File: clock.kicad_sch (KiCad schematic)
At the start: 54 parts, among them J1 USB_C_Receptacle_USB2.0_16P, J2 Conn_01x02_Pin, J4 Conn_01x02_Pin, J5 Battery, Q1 NMOS-SI2302, Q2 NPN, SW1 SW_SPST, SW2 SW_SPST, SW4 SW_SPDT, SW5 SW_SPST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

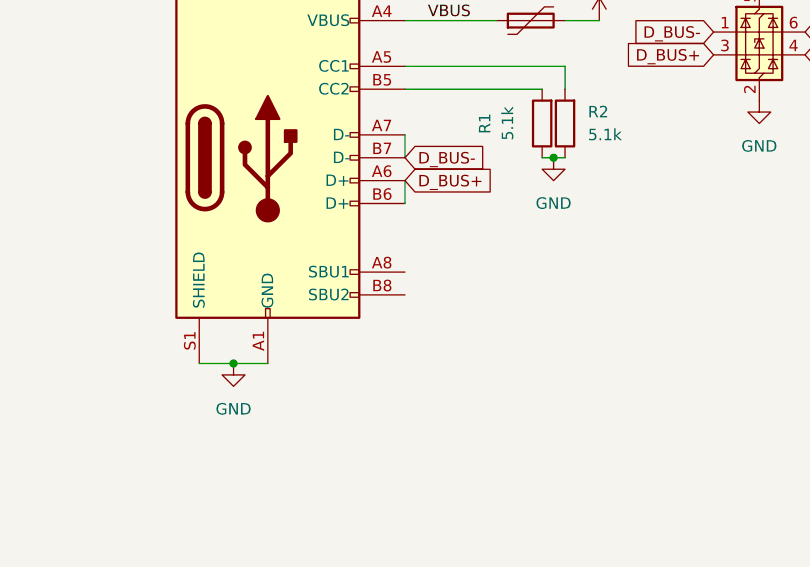
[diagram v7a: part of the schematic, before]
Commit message: sent off for production, added a few GND vias, put NRST and BOOT silkscreen on the front
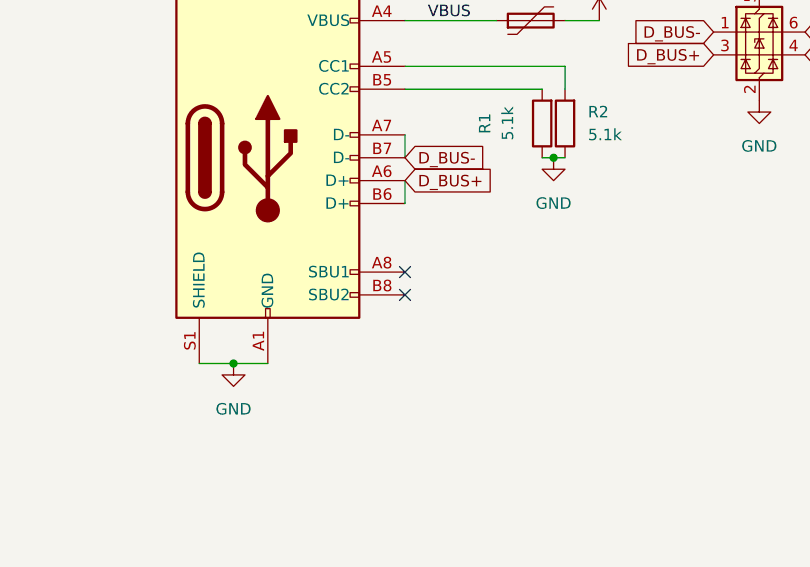
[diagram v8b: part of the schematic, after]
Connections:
- no-connect marks 19 -> 21
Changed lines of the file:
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@@
+	)
+	(no_connect
+		(at 46.99 57.15)
 	)
 	(no_connect
 		(at 43.18 158.75)
 	)
+	(no_connect
+		(at 46.99 59.69)
+	)
 	(wire
 		(pts
@@
 	(label "BAT"
 		(at 162.56 90.17 0)
-		(fields_autoplaced yes)
 		(effects
 			(font
@@
 	(label "VBUS"
 		(at 49.53 29.21 0)
-		(fields_autoplaced yes)
-		(effects
-			(font
+		(effects
+			(font
